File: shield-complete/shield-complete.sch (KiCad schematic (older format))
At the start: 10 parts, among them J1 Conn_01x03_Female, J2 Conn_01x02_Male, J3 Conn_01x04_Male, J4 Screw_Terminal_01x02

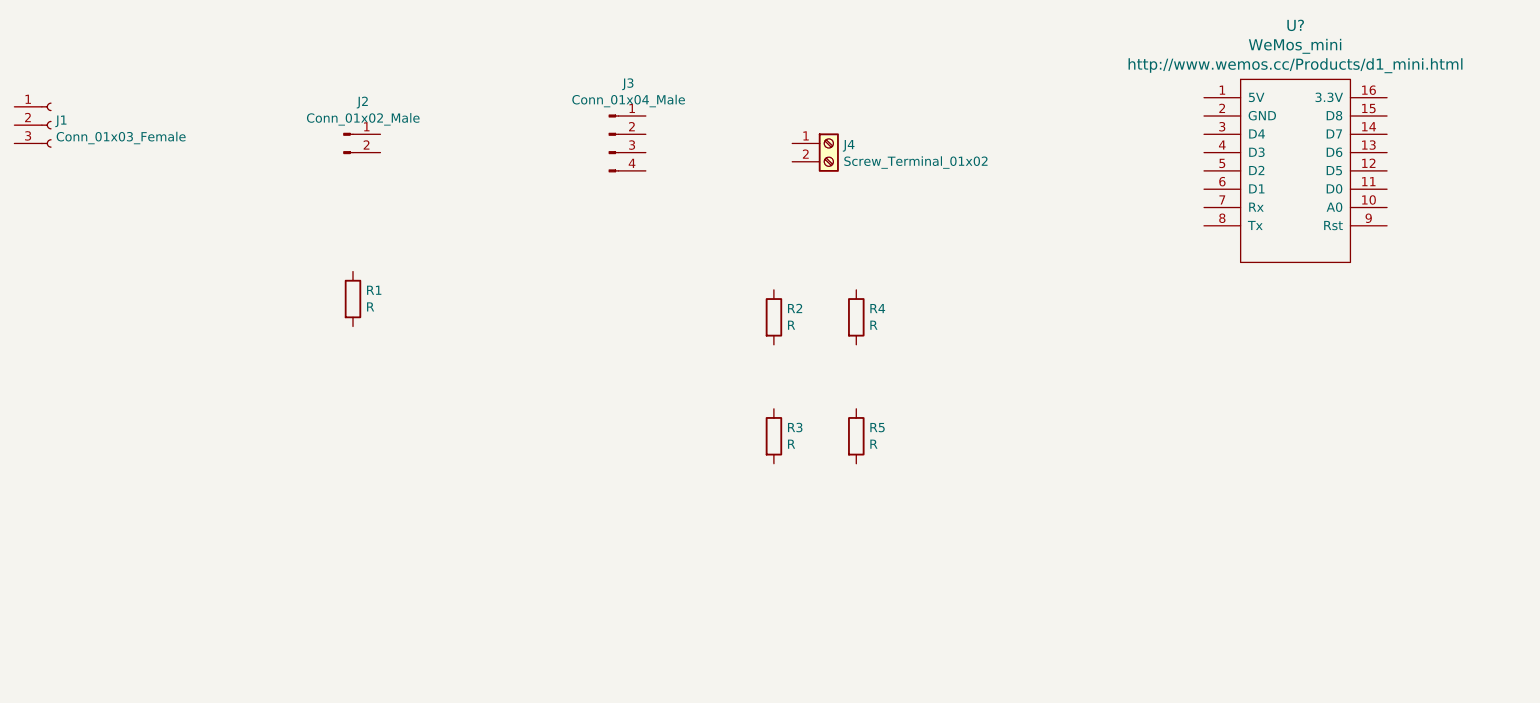
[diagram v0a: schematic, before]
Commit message: Shield as sent for manufacture
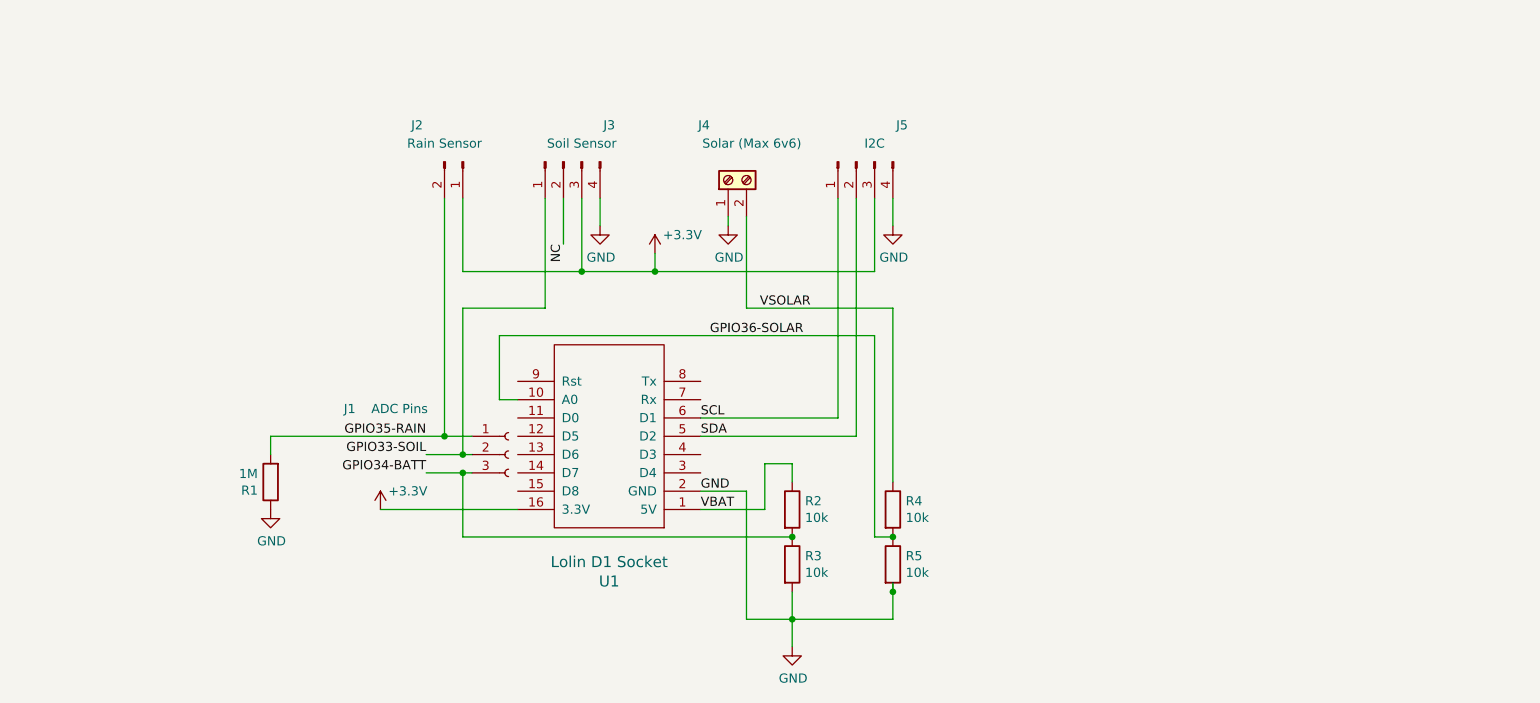
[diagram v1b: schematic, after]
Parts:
- added J5: I2C, Pin_Headers:Pin_Header_Straight_1x04_Pitch2.54mm, symbol Connector:Conn_01x04_Male
- J1: value Conn_01x03_Female -> ADC Pins
- J2: value Conn_01x02_Male -> Rain Sensor; footprint Pin_Headers:Pin_Header_Angled_1x02_Pitch2.54mm -> Pin_Headers:Pin_Header_Straight_1x02_Pitch2.54mm
- J3: value Conn_01x04_Male -> Soil Sensor; footprint Pin_Headers:Pin_Header_Angled_1x04_Pitch2.54mm -> Pin_Headers:Pin_Header_Straight_1x04_Pitch2.54mm
- J4: value Screw_Terminal_01x02 -> Solar (Max 6v6); footprint TerminalBlocks_Phoenix:TerminalBlock_Phoenix_MPT-2.54mm_2pol -> Pin_Headers:Pin_Header_Straight_1x02_Pitch2.54mm
- R1: value R -> 1M
- R2, R3, R4, R5: value R -> 10k
- U1: renamed from U?; value WeMos_mini -> Lolin D1 Socket; footprint wemos-d1-mini:wemos-d1-mini-with-pin-header-and-connector -> wemos-d1-mini:wemos-d1-mini-with-pin-header-and-connector-no-outline
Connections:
- net VBAT: now reaches U1.1 (5V)
- net VBAT: now also R2.1
- net GPIO36-SOLAR: now reaches U1.10 (A0)
- net GPIO36-SOLAR: now also R4.2, R5.1
- net +3V3: now reaches U1.16 (3.3V)
- net +3V3: now also J2.1 (Pin_1), J3.3 (Pin_3), J5.3 (Pin_3)
- net GND: now reaches U1.2 (GND)
- net GND: now also J3.4 (Pin_4), J4.1 (Pin_1), R1.1, R3.2, R5.2, J5.4 (Pin_4)
- net SDA: now reaches U1.5 (D2)
- net SDA: now also J5.2 (Pin_2)
- net SCL: now reaches U1.6 (D1)
- net SCL: now also J5.1 (Pin_1)
- net GPIO35-RAIN: now reaches J1.1 (Pin_1)
- net GPIO35-RAIN: now also J2.2 (Pin_2), R1.2
- net GPIO33-SOIL: now reaches J1.2 (Pin_2)
- net GPIO33-SOIL: now also J3.1 (Pin_1)
- net GPIO34-BATT: now reaches J1.3 (Pin_3)
- net GPIO34-BATT: now also R2.2, R3.1
- net NC: now reaches J3.2 (Pin_2)
- net VSOLAR: now reaches R4.1
- net VSOLAR: now also J4.2 (Pin_2)
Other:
- moved on the sheet: J1, J2, J3, J4, R1, R2, R3, R4, R5, U1
